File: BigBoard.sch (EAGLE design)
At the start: 12 parts

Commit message: I don't even
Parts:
- removed FRAME1: FRAME-LETTER, SparkFun-Aesthetics:FRAME-LETTER
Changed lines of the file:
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@@
 <part name="J_OUTPUT" library="SparkFun-Connectors" deviceset="M06" device="POLAR"/>
 <part name="R1" library="SparkFun-Passives" deviceset="RESISTOR" device="0805-RES" value="330"/>
-<part name="FRAME1" library="SparkFun-Aesthetics" deviceset="FRAME-LETTER" device=""/>
 <part name="J_DISPLAY" library="SparkFun-Connectors" deviceset="M05X2" device="SHD"/>
 <part name="U$2" library="bigboard" deviceset="A6278EA" device=""/>
@@
 <instance part="J_OUTPUT" gate="G$1" x="38.1" y="172.72" rot="MR180"/>
 <instance part="R1" gate="G$1" x="144.78" y="86.36" rot="R90"/>
-<instance part="FRAME1" gate="G$1" x="0" y="0"/>
-<instance part="FRAME1" gate="G$2" x="147.32" y="0"/>
 <instance part="J_DISPLAY" gate="G$1" x="22.86" y="116.84"/>
 <instance part="U$2" gate="G$1" x="147.32" y="111.76"/>

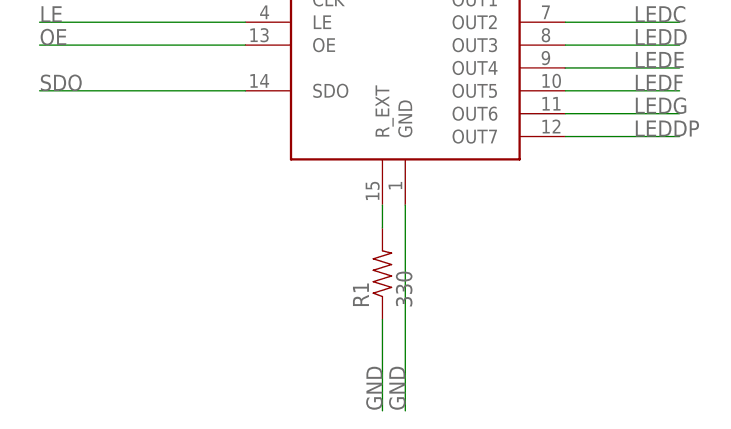
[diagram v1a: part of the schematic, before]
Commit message: Replace 0805 resistor with 0603
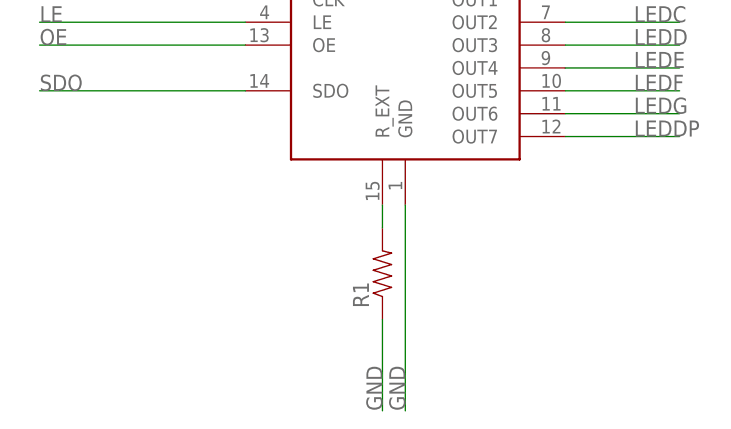
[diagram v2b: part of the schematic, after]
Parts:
- R1: value 330 -> (none); device SparkFun-Passives:RESISTOR0805-RES -> SparkFun-Passives:RESISTOR0603-RES
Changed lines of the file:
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@@
 <part name="J_INPUT" library="SparkFun-Connectors" deviceset="M06" device="POLAR"/>
 <part name="J_OUTPUT" library="SparkFun-Connectors" deviceset="M06" device="POLAR"/>
-<part name="R1" library="SparkFun-Passives" deviceset="RESISTOR" device="0805-RES" value="330"/>
 <part name="J_DISPLAY" library="SparkFun-Connectors" deviceset="M05X2" device="SHD"/>
 <part name="U$2" library="bigboard" deviceset="A6278EA" device=""/>
@@
 <part name="STANDOFF3" library="SparkFun-Electromechanical" deviceset="STAND-OFF" device=""/>
 <part name="STANDOFF4" library="SparkFun-Electromechanical" deviceset="STAND-OFF" device=""/>
+<part name="R1" library="SparkFun-Passives" deviceset="RESISTOR" device="0603-RES"/>
 </parts>
 <sheets>
@@
 <instance part="J_INPUT" gate="G$1" x="10.16" y="170.18"/>
 <instance part="J_OUTPUT" gate="G$1" x="38.1" y="172.72" rot="MR180"/>
-<instance part="R1" gate="G$1" x="144.78" y="86.36" rot="R90"/>
 <instance part="J_DISPLAY" gate="G$1" x="22.86" y="116.84"/>
 <instance part="U$2" gate="G$1" x="147.32" y="111.76"/>
@@
 <instance part="STANDOFF3" gate="G$1" x="86.36" y="170.18"/>
 <instance part="STANDOFF4" gate="G$1" x="96.52" y="170.18"/>
+<instance part="R1" gate="G$1" x="144.78" y="86.36" rot="R90"/>
 </instances>
 <busses>
@@
 </segment>
 <segment>
-<pinref part="R1" gate="G$1" pin="1"/>
 <wire x1="144.78" y1="81.28" x2="144.78" y2="71.12" width="0.1524" layer="91"/>
 <label x="144.78" y="71.12" size="1.778" layer="95" rot="R90"/>
+<pinref part="R1" gate="G$1" pin="1"/>
 </segment>
 <segment>
@@
 <net name="N$13" class="0">
 <segment>
-<pinref part="R1" gate="G$1" pin="2"/>
 <wire x1="144.78" y1="93.98" x2="144.78" y2="91.44" width="0.1524" layer="91"/>
 <pinref part="U$2" gate="G$1" pin="R_EXT"/>
+<pinref part="R1" gate="G$1" pin="2"/>
 </segment>
 </net>
